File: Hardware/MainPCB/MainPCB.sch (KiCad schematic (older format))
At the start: 2 parts

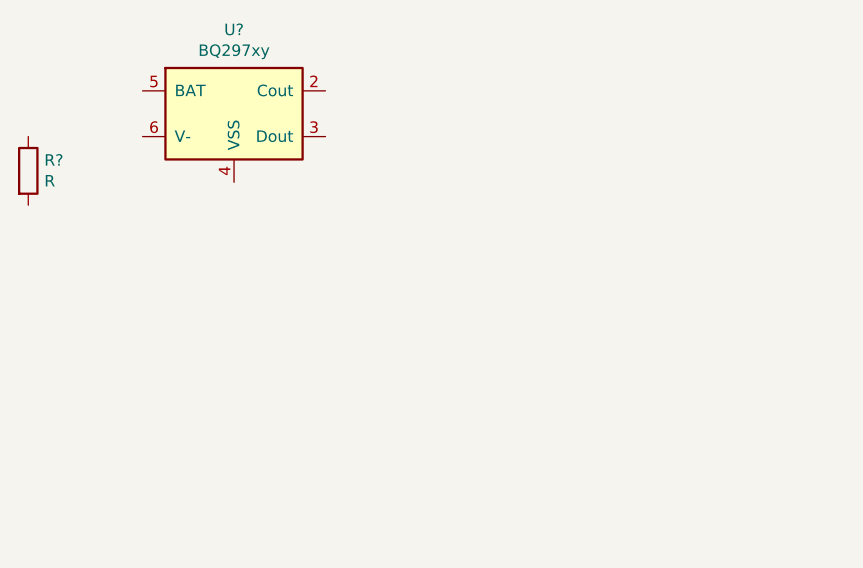
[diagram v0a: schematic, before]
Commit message: Batterij circuit beslissing genomen
Beslissing genomen over het oplaad IC, protectie IC, dual N-ch mosfets, batterij. BOM aangepast me 3 verschillende sites bij (farnell, digi-key en mouser). + IC's geplaatst in MainPCB
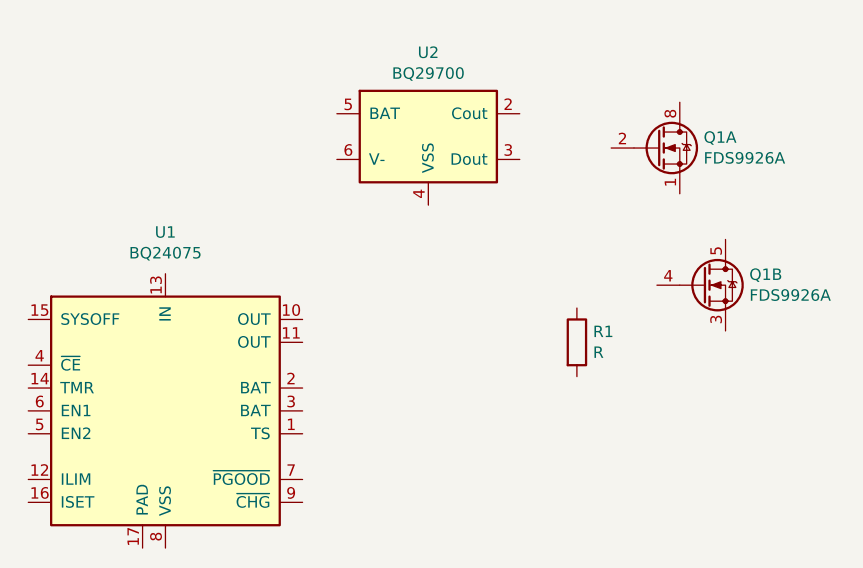
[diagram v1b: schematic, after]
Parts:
- removed R?: R, symbol Device:R
- removed U?: BQ297xy, Package_SON:WSON-6_1.5x1.5mm_P0.5mm, symbol Battery_Management:BQ297xy
- added Q1: FDS9926A, Package_SO:SOIC-8_3.9x4.9mm_P1.27mm, symbol Transistor_FET:FDS9926A
- added R1: R, Resistor_SMD:R_0612_1632Metric, symbol Device:R
- added U1: BQ24075, Package_DFN_QFN:VQFN-16-1EP_3x3mm_P0.5mm_EP1.6x1.6mm, symbol Battery_Management:BQ24075
- added U2: BQ29700, Package_SON:WSON-6_1.5x1.5mm_P0.5mm, symbol Battery_Management:BQ297xy
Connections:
- new net: Q1.7 (D1), Q1.8 (D1)
- new net: Q1.5 (D2), Q1.6 (D2)
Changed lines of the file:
@@
 $EndDescr
 $Comp
-L Device:R R?
-U 1 1 5E59146F
-P 5150 3200
-F 0 "R?" H 5220 3246 50  0000 L CNN
-F 1 "R" H 5220 3155 50  0000 L CNN
-F 2 "" V 5080 3200 50  0001 C CNN
-F 3 "~" H 5150 3200 50  0001 C CNN
-	1    5150 3200
+L Battery_Management:BQ24075 U1
+U 1 1 5E5A7039
+P 5750 4250
+F 0 "U1" H 5750 5031 50  0000 C CNN
+F 1 "BQ24075" H 5750 4940 50  0000 C CNN
+F 2 "Package_DFN_QFN:VQFN-16-1EP_3x3mm_P0.5mm_EP1.6x1.6mm" H 6000 3700 50  0001 L CNN
+F 3 "http://www.ti.com/lit/ds/symlink/bq24075.pdf" H 5950 4450 50  0001 C CNN
+	1    5750 4250
 	1    0    0    -1
 $EndComp
 $Comp
-L Battery_Management:BQ297xy U?
-U 1 1 5E592112
-P 6050 2950
-F 0 "U?" H 6050 3317 50  0000 C CNN
-F 1 "BQ297xy" H 6050 3226 50  0000 C CNN
-F 2 "Package_SON:WSON-6_1.5x1.5mm_P0.5mm" H 6050 3300 50  0001 C CNN
-F 3 "http://www.ti.com/lit/ds/symlink/bq2970.pdf" H 5800 3150 50  0001 C CNN
-	1    6050 2950
+L Device:R R1
+U 1 1 5E5A99E6
+P 7550 3950
+F 0 "R1" H 7620 3996 50  0000 L CNN
+F 1 "R" H 7620 3905 50  0000 L CNN
+F 2 "Resistor_SMD:R_0612_1632Metric" V 7480 3950 50  0001 C CNN
+F 3 "~" H 7550 3950 50  0001 C CNN
+	1    7550 3950
 	1    0    0    -1
 $EndComp
+$Comp
+L Battery_Management:BQ297xy U2
+U 1 1 5E5AA681
+P 6900 3050
+F 0 "U2" H 6900 3417 50  0000 C CNN
+F 1 "BQ29700" H 6900 3326 50  0000 C CNN
+F 2 "Package_SON:WSON-6_1.5x1.5mm_P0.5mm" H 6900 3400 50  0001 C CNN
+F 3 "http://www.ti.com/lit/ds/symlink/bq2970.pdf" H 6650 3250 50  0001 C CNN
+	1    6900 3050
+	1    0    0    -1
+$EndComp
+$Comp
+L Transistor_FET:FDS9926A Q1
+U 1 1 5E5AD09A
+P 7900 3100
+F 0 "Q1" H 8104 3146 50  0000 L CNN
+F 1 "FDS9926A" H 8104 3055 50  0000 L CNN
+F 2 "Package_SO:SOIC-8_3.9x4.9mm_P1.27mm" H 8100 3025 50  0001 L CIN
+F 3 "http://www.fairchildsemi.com/ds/FD/FDS9926A.pdf" H 7900 3100 50  0001 L CNN
+	1    7900 3100
+	1    0    0    -1
+$EndComp
+$Comp
+L Transistor_FET:FDS9926A Q1
+U 2 1 5E5AEB96
+P 8100 3700
+F 0 "Q1" H 8304 3746 50  0000 L CNN
+F 1 "FDS9926A" H 8304 3655 50  0000 L CNN
+F 2 "Package_SO:SOIC-8_3.9x4.9mm_P1.27mm" H 8300 3625 50  0001 L CIN
+F 3 "http://www.fairchildsemi.com/ds/FD/FDS9926A.pdf" H 8100 3700 50  0001 L CNN
+	2    8100 3700
+	1    0    0    -1
+$EndComp

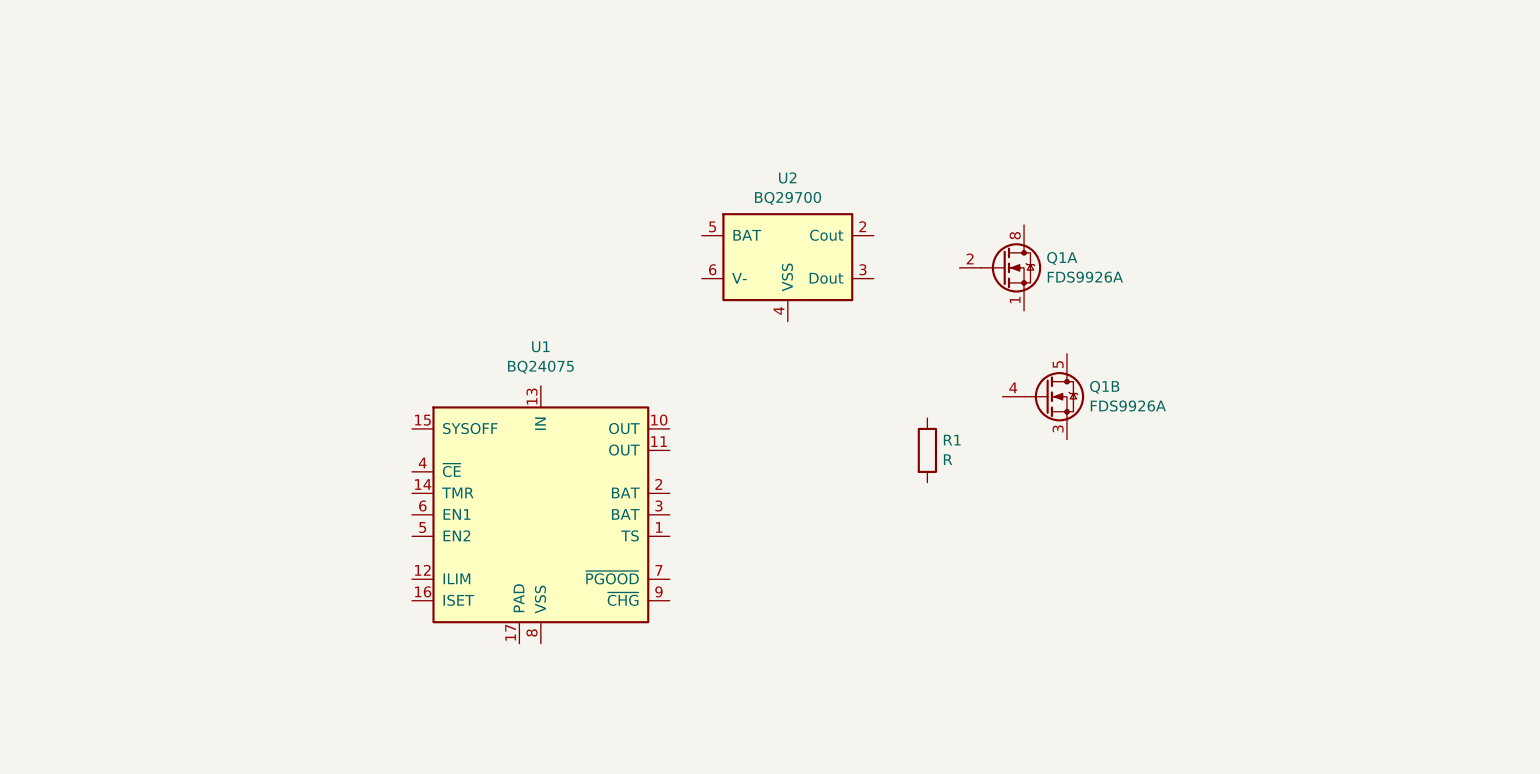
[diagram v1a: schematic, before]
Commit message: Changed battery holder 1043 TH to 1042 SMD
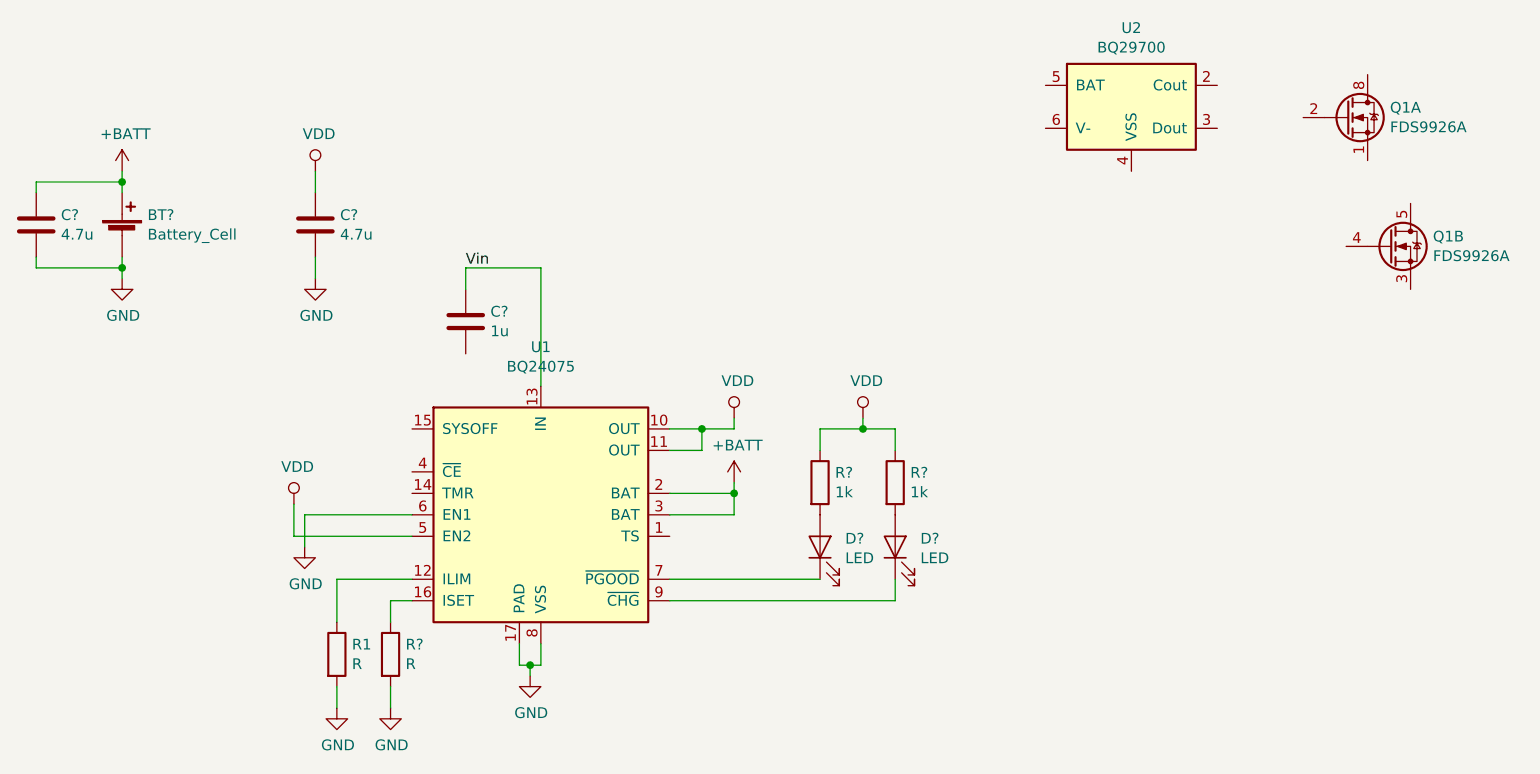
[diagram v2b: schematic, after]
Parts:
- added BT?: Battery_Cell, Battery:BatteryHolder_Keystone_1042_1x18650, symbol Device:Battery_Cell
- added C?: 1u, symbol Device:C
- added C? (x2): 4.7u, symbol Device:C
- added D? (x2): LED, symbol Device:LED
- added R?: R, Resistor_SMD:R_0612_1632Metric, symbol Device:R
- added R? (x2): 1k, Resistor_SMD:R_0612_1632Metric, symbol Device:R
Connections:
- net VDD: now reaches U1.10 (OUT)
- net VDD: now also U1.11 (OUT), U1.5 (EN2), C?.1, R?.1, R?.1
- net at U1.12 (ILIM): now also R1.1
- net Vin: now reaches U1.13 (IN)
- net Vin: now also C?.1
- net at U1.16 (ISET): now also R?.1
- net GND: now reaches U1.17 (PAD)
- net GND: now also R1.2, U1.6 (EN1), U1.8 (VSS), BT?.2 (-), C?.2, C?.2, R?.2
- net +BATT: now reaches U1.2 (BAT)
- net +BATT: now also U1.3 (BAT), BT?.1 (+), C?.1
- net at U1.7 (~PGOOD): now also D?.1 (K)
- net at U1.9 (~CHG): now also D?.1 (K)
- new net: D?.2 (A), R?.2 (x2)
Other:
- moved on the sheet: Q1A, Q1B, R1, U2

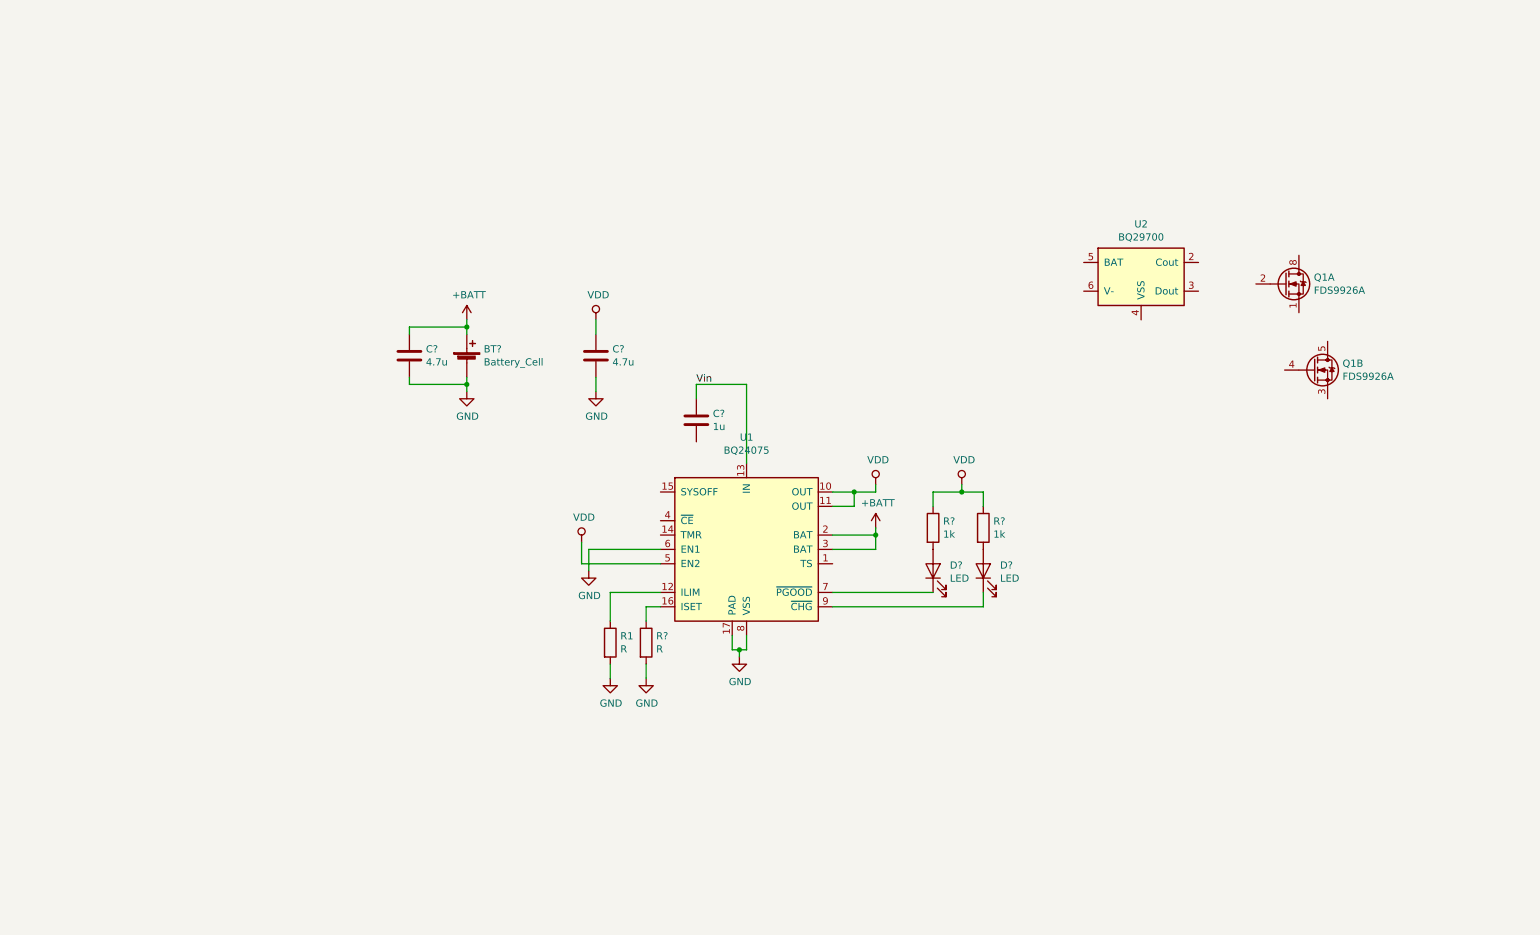
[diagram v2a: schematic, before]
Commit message: Toevoeging LDO
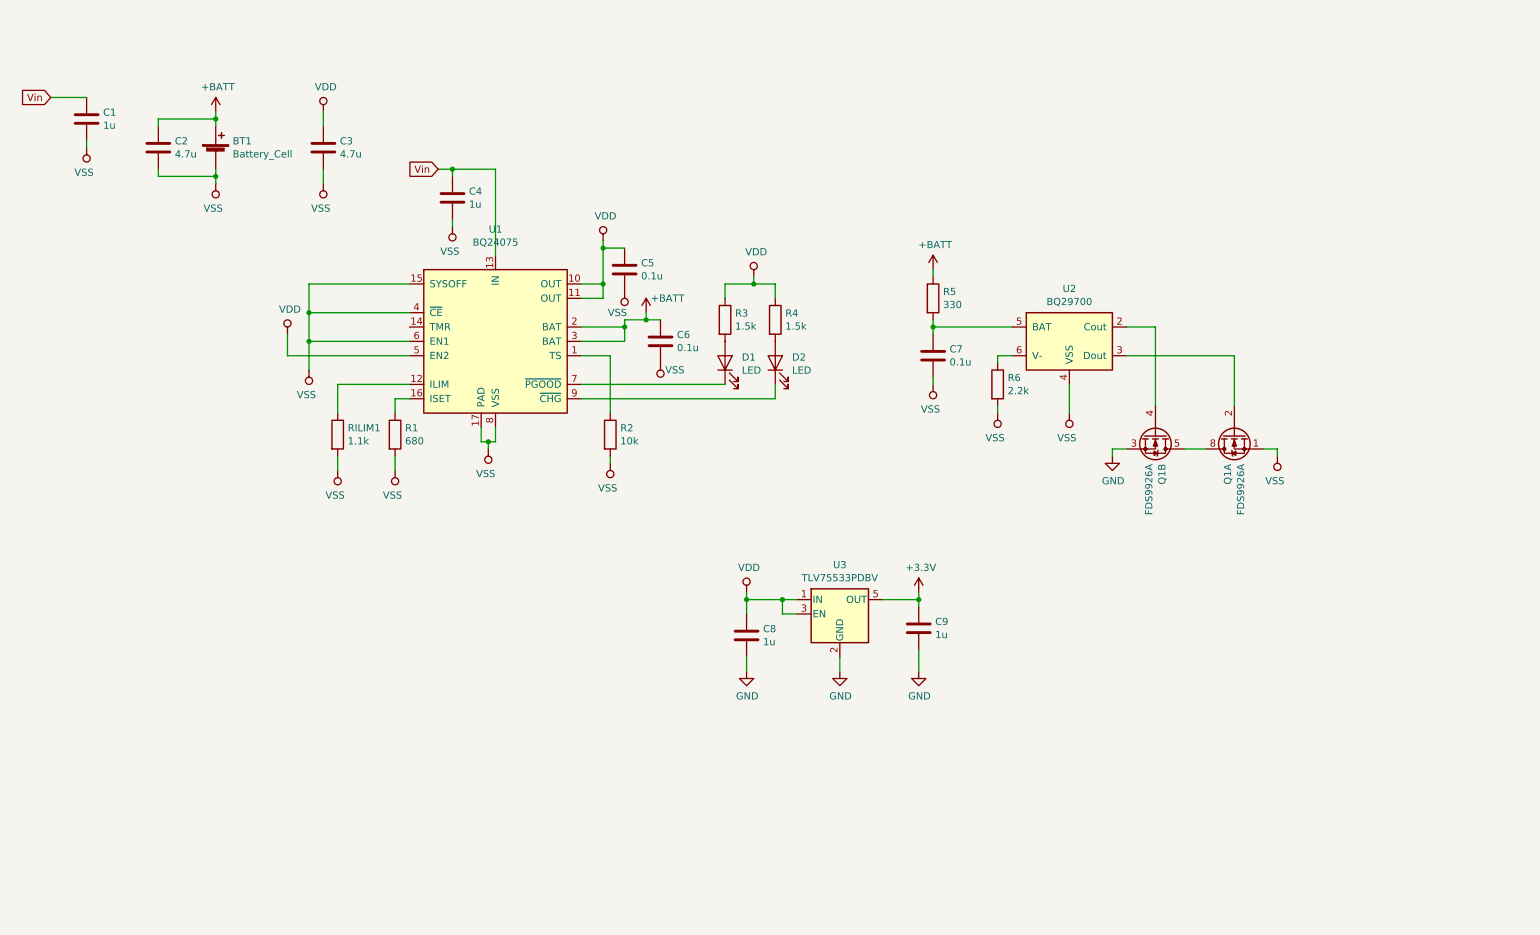
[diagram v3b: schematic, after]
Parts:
- added C1, C8, C9: 1u, symbol Device:C
- added C5, C6, C7: 0.1u, symbol Device:C
- added R2: 10k, Resistor_SMD:R_0612_1632Metric, symbol Device:R
- added R5: 330, Resistor_SMD:R_0612_1632Metric, symbol Device:R
- added R6: 2.2k, Resistor_SMD:R_0612_1632Metric, symbol Device:R
- added U3: TLV75533PDBV, Package_TO_SOT_SMD:SOT-23-5, symbol Regulator_Linear:TLV75533PDBV
- R1: renamed from R?; value R -> 680
- R3, R4: renamed from R?; value 1k -> 1.5k
- RILIM1: renamed from R1; value R -> 1.1k
- gave numbers to parts that had none: 6
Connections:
- net +BATT: now also C6.1, R5.1
- net GND: now also Q1.3 (S2), C8.2, C9.2, U3.2 (GND); no longer BT1.2 (-), C2.2, C3.2, R1.2, RILIM1.2, U1.17 (PAD), U1.6 (EN1), U1.8 (VSS)
- net VDD: now also C5.1, C8.1, U3.1 (IN), U3.3 (EN)
- net Vin: now also C1.1
- net at U1.1 (TS): now also R2.1
- net VSS: now reaches U1.15 (SYSOFF)
- net VSS: now also BT1.2 (-), C2.2, C3.2, C4.2, Q1.1 (S1), R1.2, RILIM1.2, U1.17 (PAD), U1.4 (~CE), U1.6 (EN1), U1.8 (VSS), U2.4 (VSS), C1.2, C5.2, C6.2, C7.2, R2.2, R6.2
- net at U2.2 (Cout): now also Q1.4 (G2)
- net at U2.3 (Dout): now also Q1.2 (G1)
- net at U2.5 (BAT): now also C7.1, R5.2
- net at U2.6 (V-): now also R6.1
- net at Q1.7 (D1), Q1.8 (D1): now also Q1.5 (D2), Q1.6 (D2)
- new net +3V3: C9.1, U3.5 (OUT)
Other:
- moved on the sheet: BT1, C2, C3, C4, D1, D2, Q1A, Q1B, R1, R3, R4, RILIM1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

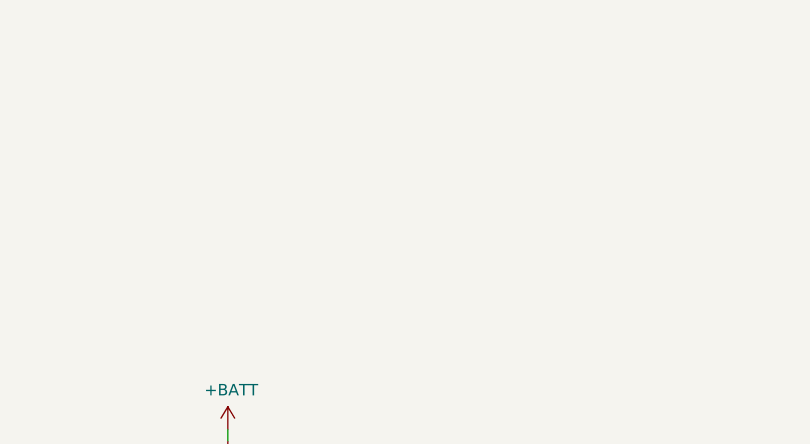
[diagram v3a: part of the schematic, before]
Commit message: Toevoeging 1 load switch
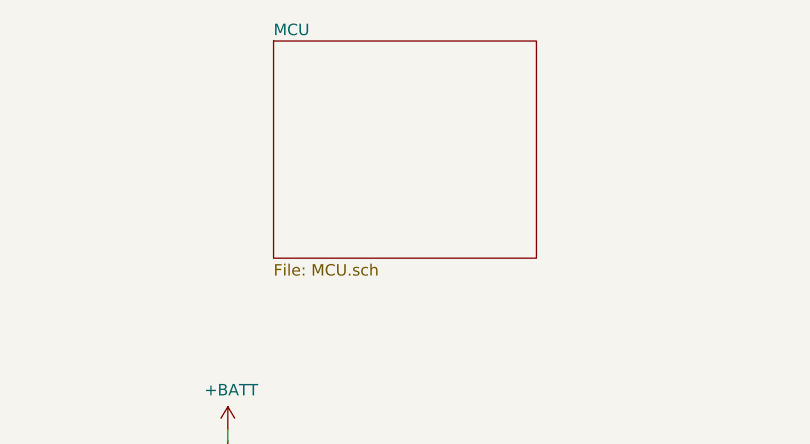
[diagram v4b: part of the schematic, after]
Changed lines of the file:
@@
 $Descr A4 11693 8268
 encoding utf-8
-Sheet 1 1
+Sheet 1 2
 Title ""
 Date ""
@@
 	6950 4550 6950 4600
 Connection ~ 6950 4600
+$Sheet
+S 7250 600  1150 950
+U 5E6059B5
+F0 "MCU" 50
+F1 "MCU.sch" 50
+$EndSheet
 $EndSCHEMATC
